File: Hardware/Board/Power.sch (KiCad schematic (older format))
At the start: 84 parts, among them Q100 2N7002, Q102 2N7002, Q103 2N7002, Q104 2N7002, U100 MAX17572, U101 MAX17572, U102 MAX17572, U104 MAX17574, U105 MAX17574

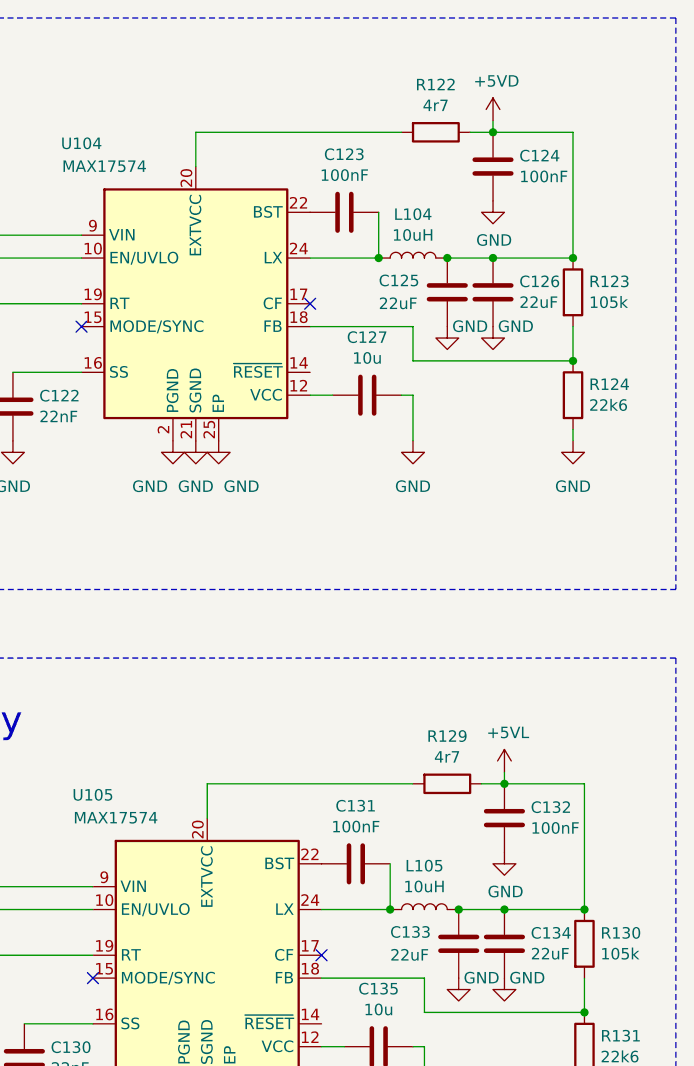
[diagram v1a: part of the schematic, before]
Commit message: Power Supply gerouted, Fehlerkorrektur
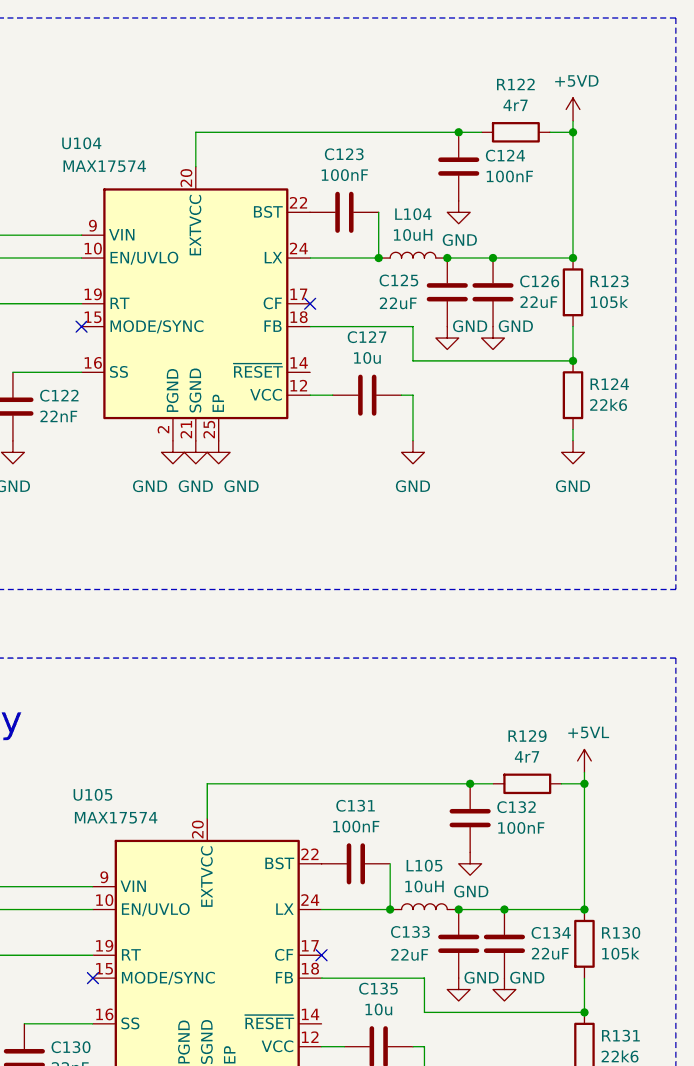
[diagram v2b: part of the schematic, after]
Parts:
- C109: footprint Capacitor_SMD:C_1210_3225Metric -> Capacitor_SMD:C_0603_1608Metric
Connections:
- net +5VD: no longer C124.1
- net +5VL: no longer C132.1
- net at R122.2, U104.20 (EXTVCC): now also C124.1
- net at R129.2, U105.20 (EXTVCC): now also C132.1
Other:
- moved on the sheet: C124, C132, R122, R129
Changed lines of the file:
@@
-$EndComp
-$Comp
-L Womo-rescue:+5VD-power #PWR0161
-U 1 1 5CA4F95B
-P 10800 1250
-AR Path="/5C8BBC9A/5CA4F95B" Ref="#PWR0161"  Part="1"
-AR Path="/5E0C5EEA/5CA4F95B" Ref="#PWR?"  Part="1"
-F 0 "#PWR0161" H 10800 1100 50  0001 C CNN
-F 1 "+5VD" H 10815 1423 50  0000 C CNN
-F 2 "" H 10800 1250 50  0001 C CNN
-F 3 "" H 10800 1250 50  0001 C CNN
-	1    10800 1250
-	1    0    0    -1
 $EndComp
 $Comp
@@
 F 3 "~" H 7300 1900 50  0001 C CNN
 	1    7300 1900
-	1    0    0    -1
-$EndComp
-$Comp
-L Womo-rescue:C-Device C124
-U 1 1 5CA4FBFF
-P 10800 1450
-AR Path="/5C8BBC9A/5CA4FBFF" Ref="C124"  Part="1"
-AR Path="/5E0C5EEA/5CA4FBFF" Ref="C?"  Part="1"
-F 0 "C124" H 10915 1496 50  0000 L CNN
-F 1 "100nF" H 10915 1405 50  0000 L CNN
-F 2 "Capacitor_SMD:C_0603_1608Metric" H 10838 1300 50  0001 C CNN
-F 3 "~" H 10800 1450 50  0001 C CNN
-	1    10800 1450
 	1    0    0    -1
 $EndComp
@@
 	1    0    0    -1
 $EndComp
-$Comp
-L Womo-rescue:R-Device R122
-U 1 1 5CA5005E
-P 10550 1300
-AR Path="/5C8BBC9A/5CA5005E" Ref="R122"  Part="1"
-AR Path="/5E0C5EEA/5CA5005E" Ref="R?"  Part="1"
-F 0 "R122" V 10343 1300 50  0000 C CNN
-F 1 "4r7" V 10434 1300 50  0000 C CNN
-F 2 "Resistor_SMD:R_0603_1608Metric" V 10480 1300 50  0001 C CNN
-F 3 "~" H 10550 1300 50  0001 C CNN
-	1    10550 1300
-	0    1    1    0
-$EndComp
 Wire Wire Line
 	10000 1850 10300 1850
@@
 $EndComp
 Wire Wire Line
-	10800 1250 10800 1300
-Wire Wire Line
-	10800 1300 10700 1300
-Wire Wire Line
 	9000 2350 8700 2350
-Connection ~ 10800 1300
-$Comp
-L Womo-rescue:GND-power #PWR0169
-U 1 1 5CA51A11
-P 10800 1600
-AR Path="/5C8BBC9A/5CA51A11" Ref="#PWR0169"  Part="1"
-AR Path="/5E0C5EEA/5CA51A11" Ref="#PWR?"  Part="1"
-F 0 "#PWR0169" H 10800 1350 50  0001 C CNN
-F 1 "GND" H 10805 1427 50  0000 C CNN
-F 2 "" H 10800 1600 50  0001 C CNN
-F 3 "" H 10800 1600 50  0001 C CNN
-	1    10800 1600
-	1    0    0    -1
-$EndComp
-Wire Wire Line
-	11150 1300 10800 1300
 Wire Wire Line
 	11150 1300 11150 1850
 Wire Wire Line
 	9500 1450 9500 1300
-Wire Wire Line
-	9500 1300 10400 1300
 Wire Wire Line
 	10000 2450 10100 2450
@@
 F 0 "C109" V 4550 5250 50  0000 C CNN
 F 1 "4u7" V 4650 5300 50  0000 C CNN
-F 2 "Capacitor_SMD:C_1210_3225Metric" H 4438 5200 50  0001 C CNN
+F 2 "Capacitor_SMD:C_0603_1608Metric" H 4438 5200 50  0001 C CNN
 F 3 "~" H 4400 5350 50  0001 C CNN
 	1    4400 5350
@@
 L Womo-rescue:C-Device C132
 U 1 1 5D9244C7
-P 10850 4300
+P 10700 4300
 AR Path="/5C8BBC9A/5D9244C7" Ref="C132"  Part="1"
 AR Path="/5E0C5EEA/5D9244C7" Ref="C?"  Part="1"
-F 0 "C132" H 10965 4346 50  0000 L CNN
-F 1 "100nF" H 10965 4255 50  0000 L CNN
-F 2 "Capacitor_SMD:C_0603_1608Metric" H 10888 4150 50  0001 C CNN
-F 3 "~" H 10850 4300 50  0001 C CNN
-	1    10850 4300
+F 0 "C132" H 10815 4346 50  0000 L CNN
+F 1 "100nF" H 10815 4255 50  0000 L CNN
+F 2 "Capacitor_SMD:C_0603_1608Metric" H 10738 4150 50  0001 C CNN
+F 3 "~" H 10700 4300 50  0001 C CNN
+	1    10700 4300
 	1    0    0    -1
 $EndComp
@@
 	1    0    0    -1
 $EndComp
-$Comp
-L Womo-rescue:R-Device R129
-U 1 1 5D9244F8
-P 10600 4150
-AR Path="/5C8BBC9A/5D9244F8" Ref="R129"  Part="1"
-AR Path="/5E0C5EEA/5D9244F8" Ref="R?"  Part="1"
-F 0 "R129" V 10393 4150 50  0000 C CNN
-F 1 "4r7" V 10484 4150 50  0000 C CNN
-F 2 "Resistor_SMD:R_0603_1608Metric" V 10530 4150 50  0001 C CNN
-F 3 "~" H 10600 4150 50  0001 C CNN
-	1    10600 4150
-	0    1    1    0
-$EndComp
 Wire Wire Line
 	10050 4700 10350 4700
@@
 $EndComp
 Wire Wire Line
-	10850 4100 10850 4150
-Wire Wire Line
-	10850 4150 10750 4150
-Wire Wire Line
 	9050 5200 8750 5200
-Connection ~ 10850 4150
 $Comp
 L Womo-rescue:GND-power #PWR0224
 U 1 1 5D924526
-P 10850 4450
+P 10700 4450
 AR Path="/5C8BBC9A/5D924526" Ref="#PWR0224"  Part="1"
 AR Path="/5E0C5EEA/5D924526" Ref="#PWR?"  Part="1"
-F 0 "#PWR0224" H 10850 4200 50  0001 C CNN
-F 1 "GND" H 10855 4277 50  0000 C CNN
-F 2 "" H 10850 4450 50  0001 C CNN
-F 3 "" H 10850 4450 50  0001 C CNN
-	1    10850 4450
-	1    0    0    -1
-$EndComp
-Wire Wire Line
-	11200 4150 10850 4150
+F 0 "#PWR0224" H 10700 4200 50  0001 C CNN
+F 1 "GND" H 10705 4277 50  0000 C CNN
+F 2 "" H 10700 4450 50  0001 C CNN
+F 3 "" H 10700 4450 50  0001 C CNN
+	1    10700 4450
+	1    0    0    -1
+$EndComp
 Wire Wire Line
 	11200 4150 11200 4700
 Wire Wire Line
 	9550 4300 9550 4150
-Wire Wire Line
-	9550 4150 10450 4150
 Wire Wire Line
 	10050 5300 10150 5300
@@
 F 3 "https://www.fairchildsemi.com/datasheets/2N/2N7002.pdf" H 7800 5250 50  0001 L CNN
 	1    7800 5250
-	1    0    0    -1
-$EndComp
-$Comp
-L Womo-rescue:+5VL-power #PWR0235
-U 1 1 5D99488F
-P 10850 4100
-F 0 "#PWR0235" H 10850 3950 50  0001 C CNN
-F 1 "+5VL" H 10865 4273 50  0000 C CNN
-F 2 "" H 10850 4100 50  0001 C CNN
-F 3 "" H 10850 4100 50  0001 C CNN
-	1    10850 4100
 	1    0    0    -1
 $EndComp
@@
 Wire Wire Line
 	7150 5250 7050 5250
+$Comp
+L Womo-rescue:GND-power #PWR0169
+U 1 1 5CA51A11
+P 10650 1600
+AR Path="/5C8BBC9A/5CA51A11" Ref="#PWR0169"  Part="1"
+AR Path="/5E0C5EEA/5CA51A11" Ref="#PWR?"  Part="1"
+F 0 "#PWR0169" H 10650 1350 50  0001 C CNN
+F 1 "GND" H 10655 1427 50  0000 C CNN
+F 2 "" H 10650 1600 50  0001 C CNN
+F 3 "" H 10650 1600 50  0001 C CNN
+	1    10650 1600
+	1    0    0    -1
+$EndComp
+Connection ~ 10650 1300
+Wire Wire Line
+	11150 1250 11150 1300
+$Comp
+L Womo-rescue:C-Device C124
+U 1 1 5CA4FBFF
+P 10650 1450
+AR Path="/5C8BBC9A/5CA4FBFF" Ref="C124"  Part="1"
+AR Path="/5E0C5EEA/5CA4FBFF" Ref="C?"  Part="1"
+F 0 "C124" H 10765 1496 50  0000 L CNN
+F 1 "100nF" H 10765 1405 50  0000 L CNN
+F 2 "Capacitor_SMD:C_0603_1608Metric" H 10688 1300 50  0001 C CNN
+F 3 "~" H 10650 1450 50  0001 C CNN
+	1    10650 1450
+	1    0    0    -1
+$EndComp
+$Comp
+L Womo-rescue:+5VD-power #PWR0161
+U 1 1 5CA4F95B
+P 11150 1250
+AR Path="/5C8BBC9A/5CA4F95B" Ref="#PWR0161"  Part="1"
+AR Path="/5E0C5EEA/5CA4F95B" Ref="#PWR?"  Part="1"
+F 0 "#PWR0161" H 11150 1100 50  0001 C CNN
+F 1 "+5VD" H 11165 1423 50  0000 C CNN
+F 2 "" H 11150 1250 50  0001 C CNN
+F 3 "" H 11150 1250 50  0001 C CNN
+	1    11150 1250
+	1    0    0    -1
+$EndComp
+$Comp
+L Womo-rescue:R-Device R122
+U 1 1 5CA5005E
+P 10900 1300
+AR Path="/5C8BBC9A/5CA5005E" Ref="R122"  Part="1"
+AR Path="/5E0C5EEA/5CA5005E" Ref="R?"  Part="1"
+F 0 "R122" V 10693 1300 50  0000 C CNN
+F 1 "4r7" V 10784 1300 50  0000 C CNN
+F 2 "Resistor_SMD:R_0603_1608Metric" V 10830 1300 50  0001 C CNN
+F 3 "~" H 10900 1300 50  0001 C CNN
+	1    10900 1300
+	0    1    1    0
+$EndComp
+Connection ~ 10700 4150
+Wire Wire Line
+	11200 4100 11200 4150
+$Comp
+L Womo-rescue:R-Device R129
+U 1 1 5D9244F8
+P 10950 4150
+AR Path="/5C8BBC9A/5D9244F8" Ref="R129"  Part="1"
+AR Path="/5E0C5EEA/5D9244F8" Ref="R?"  Part="1"
+F 0 "R129" V 10743 4150 50  0000 C CNN
+F 1 "4r7" V 10834 4150 50  0000 C CNN
+F 2 "Resistor_SMD:R_0603_1608Metric" V 10880 4150 50  0001 C CNN
+F 3 "~" H 10950 4150 50  0001 C CNN
+	1    10950 4150
+	0    1    1    0
+$EndComp
+$Comp
+L Womo-rescue:+5VL-power #PWR0235
+U 1 1 5D99488F
+P 11200 4100
+F 0 "#PWR0235" H 11200 3950 50  0001 C CNN
+F 1 "+5VL" H 11215 4273 50  0000 C CNN
+F 2 "" H 11200 4100 50  0001 C CNN
+F 3 "" H 11200 4100 50  0001 C CNN
+	1    11200 4100
+	1    0    0    -1
+$EndComp
+Wire Wire Line
+	11200 4150 11100 4150
+Wire Wire Line
+	9550 4150 10700 4150
+Wire Wire Line
+	10800 4150 10700 4150
+Wire Wire Line
+	9500 1300 10650 1300
+Wire Wire Line
+	10750 1300 10650 1300
+Wire Wire Line
+	11150 1300 11050 1300
+Connection ~ 11200 4150
+Connection ~ 11150 1300
 $EndSCHEMATC

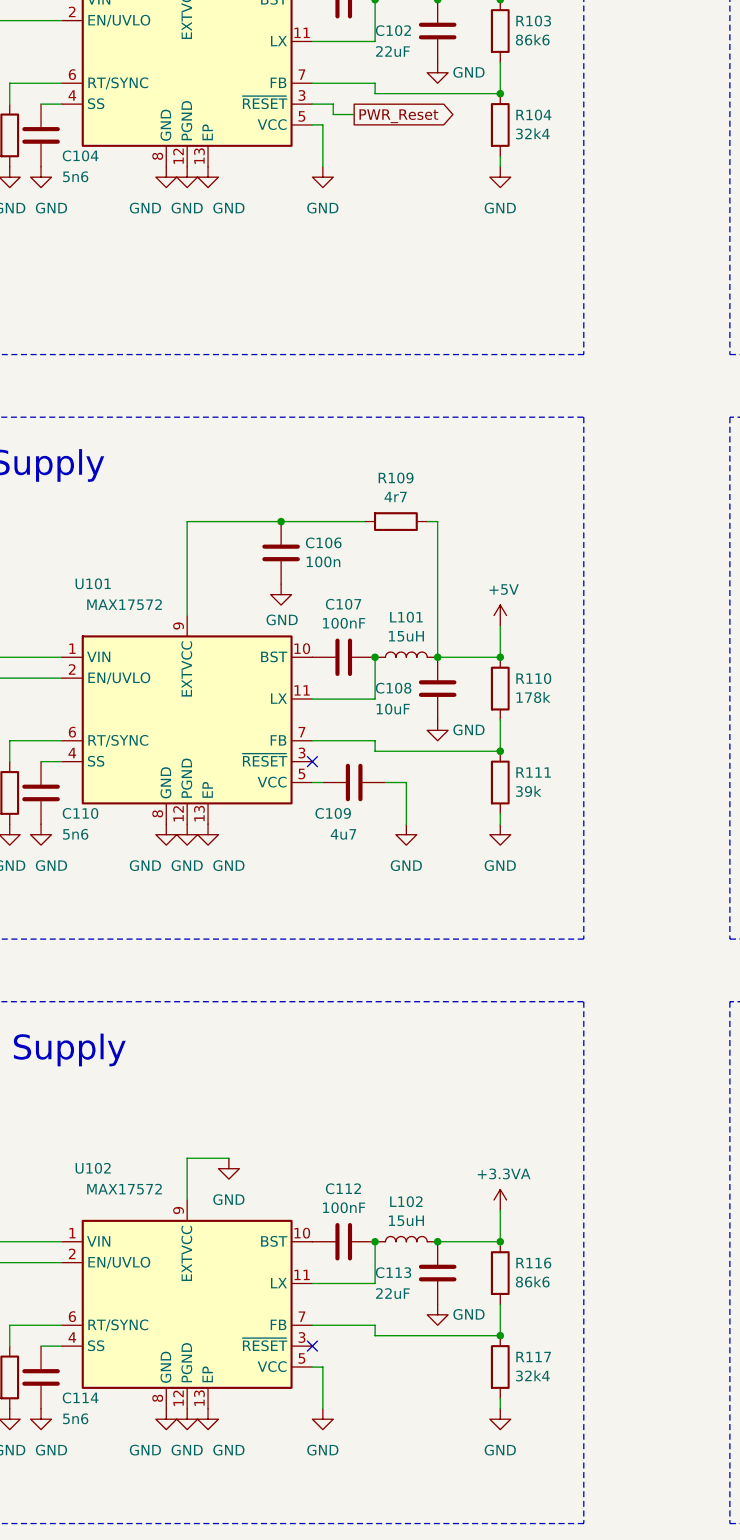
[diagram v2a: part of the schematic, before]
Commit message: Fix: behinderten Masse Bug an 3v3 Regler Mainunit und Displayboard
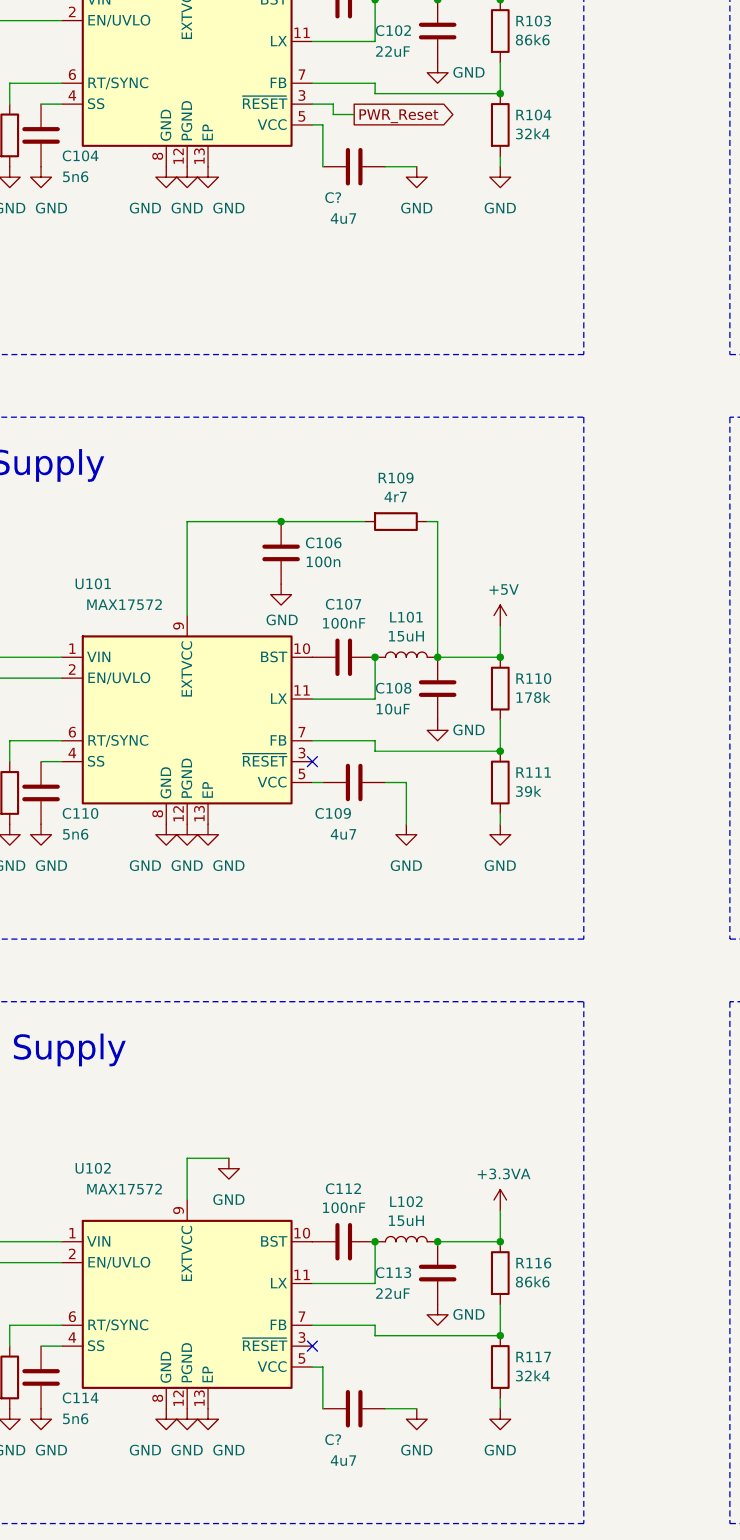
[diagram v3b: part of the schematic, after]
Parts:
- added C? (x2): 4u7, Capacitor_SMD:C_0603_1608Metric, symbol Womo-rescue:C-Device
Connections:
- net GND: now also C?.1, C?.1; no longer U100.5 (VCC), U102.5 (VCC)
- new net: C?.2, U100.5 (VCC)
- new net: C?.2, U102.5 (VCC)
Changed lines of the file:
@@
 EESchema Schematic File Version 4
 LIBS:Womo-cache
-EELAYER 29 0
+EELAYER 30 0
 EELAYER END
 $Descr A3 16535 11693
@@
 L Womo-rescue:GND-power #PWR0185
 U 1 1 5CA770FA
-P 4250 2400
+P 4700 2400
 AR Path="/5C8BBC9A/5CA770FA" Ref="#PWR0185"  Part="1"
 AR Path="/5E0C5EEA/5CA770FA" Ref="#PWR?"  Part="1"
-F 0 "#PWR0185" H 4250 2150 50  0001 C CNN
-F 1 "GND" H 4250 2200 50  0000 C CNN
-F 2 "" H 4250 2400 50  0001 C CNN
-F 3 "" H 4250 2400 50  0001 C CNN
-	1    4250 2400
+F 0 "#PWR0185" H 4700 2150 50  0001 C CNN
+F 1 "GND" H 4700 2200 50  0000 C CNN
+F 2 "" H 4700 2400 50  0001 C CNN
+F 3 "" H 4700 2400 50  0001 C CNN
+	1    4700 2400
 	1    0    0    -1
 $EndComp
@@
 Wire Wire Line
 	4800 7550 5100 7550
-$Comp
-L Womo-rescue:GND-power #PWR0188
-U 1 1 5CA78561
-P 4250 8350
-AR Path="/5C8BBC9A/5CA78561" Ref="#PWR0188"  Part="1"
-AR Path="/5E0C5EEA/5CA78561" Ref="#PWR?"  Part="1"
-F 0 "#PWR0188" H 4250 8100 50  0001 C CNN
-F 1 "GND" H 4250 8150 50  0000 C CNN
-F 2 "" H 4250 8350 50  0001 C CNN
-F 3 "" H 4250 8350 50  0001 C CNN
-	1    4250 8350
-	1    0    0    -1
-$EndComp
 Wire Wire Line
 	4200 8150 4250 8150
@@
 Connection ~ 11200 4150
 Connection ~ 11150 1300
+$Comp
+L Womo-rescue:GND-power #PWR0188
+U 1 1 5CA78561
+P 4700 8350
+AR Path="/5C8BBC9A/5CA78561" Ref="#PWR0188"  Part="1"
+AR Path="/5E0C5EEA/5CA78561" Ref="#PWR?"  Part="1"
+F 0 "#PWR0188" H 4700 8100 50  0001 C CNN
+F 1 "GND" H 4700 8150 50  0000 C CNN
+F 2 "" H 4700 8350 50  0001 C CNN
+F 3 "" H 4700 8350 50  0001 C CNN
+	1    4700 8350
+	1    0    0    -1
+$EndComp
+$Comp
+L Womo-rescue:C-Device C?
+U 1 1 5E15C6EC
+P 4400 2400
+AR Path="/5C8BBC9A/5E15C6EC" Ref="C?"  Part="1"
+AR Path="/5E0C5EEA/5E15C6EC" Ref="C?"  Part="1"
+F 0 "C?" V 4550 2300 50  0000 C CNN
+F 1 "4u7" V 4650 2350 50  0000 C CNN
+F 2 "Capacitor_SMD:C_0603_1608Metric" H 4438 2250 50  0001 C CNN
+F 3 "~" H 4400 2400 50  0001 C CNN
+	1    4400 2400
+	0    1    1    0
+$EndComp
+$Comp
+L Womo-rescue:C-Device C?
+U 1 1 5E19DC38
+P 4400 8350
+AR Path="/5C8BBC9A/5E19DC38" Ref="C?"  Part="1"
+AR Path="/5E0C5EEA/5E19DC38" Ref="C?"  Part="1"
+F 0 "C?" V 4550 8250 50  0000 C CNN
+F 1 "4u7" V 4650 8300 50  0000 C CNN
+F 2 "Capacitor_SMD:C_0603_1608Metric" H 4438 8200 50  0001 C CNN
+F 3 "~" H 4400 8350 50  0001 C CNN
+	1    4400 8350
+	0    1    1    0
+$EndComp
+Wire Wire Line
+	4700 8350 4550 8350
+Wire Wire Line
+	4700 2400 4550 2400
 $EndSCHEMATC
